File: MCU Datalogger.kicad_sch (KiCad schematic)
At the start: 25 parts, among them U1 24LC1025, U2 DS1337S_, U3 24LC1025, U4 ATMEGA328P-AU, Y1 32.768 KHZ, Y2 16 MHZ

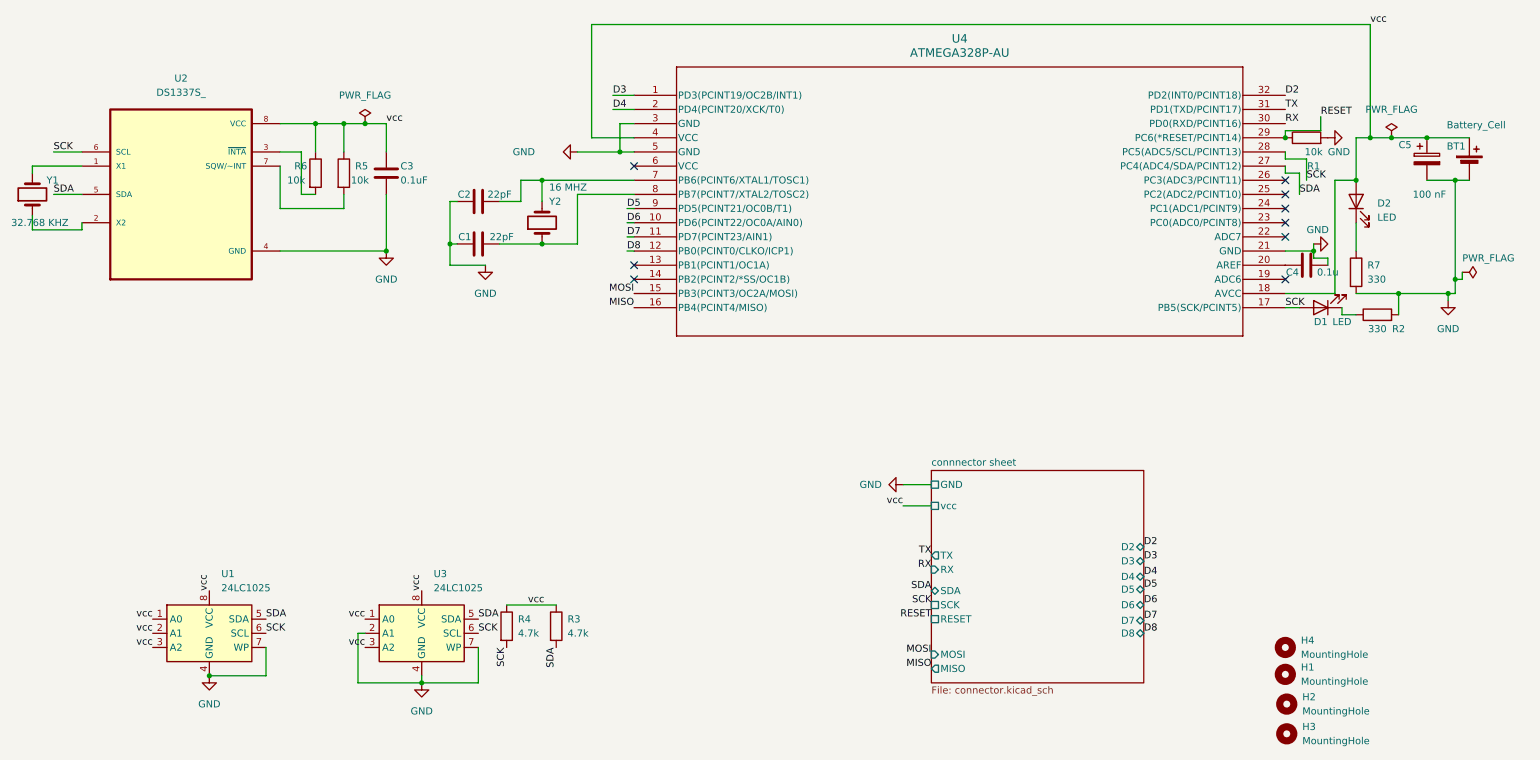
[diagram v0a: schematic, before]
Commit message: fixed two defects in schematic
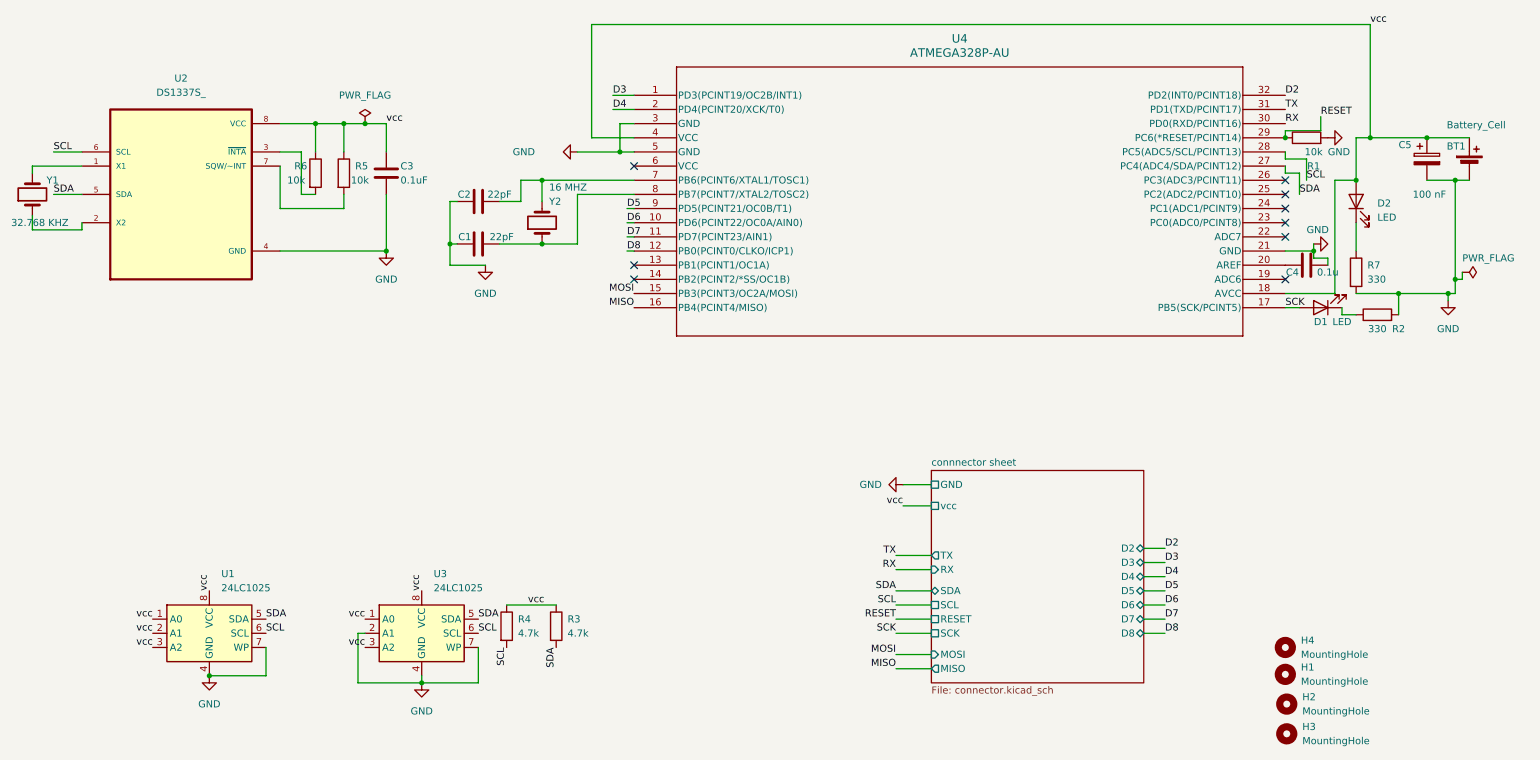
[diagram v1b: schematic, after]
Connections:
- net SCK: no longer R4.2, U1.6 (SCL), U2.6 (SCL), U3.6 (SCL), U4.28 (PC5(ADC5/SCL/PCINT13))
- new net SCL: R4.2, U1.6 (SCL), U2.6 (SCL), U3.6 (SCL), U4.28 (PC5(ADC5/SCL/PCINT13))
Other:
- sheet connnector sheet ports: added SCL; removed none
